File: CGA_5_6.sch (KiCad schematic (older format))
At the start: 34 parts, among them Q1 2N3904, U13 74LS08, U14 74S32, U15 74LS00, U20 74LS04, U21 74LS174, U24 74LS244, U41 74LS08, U42 74LS86, U43 74S74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

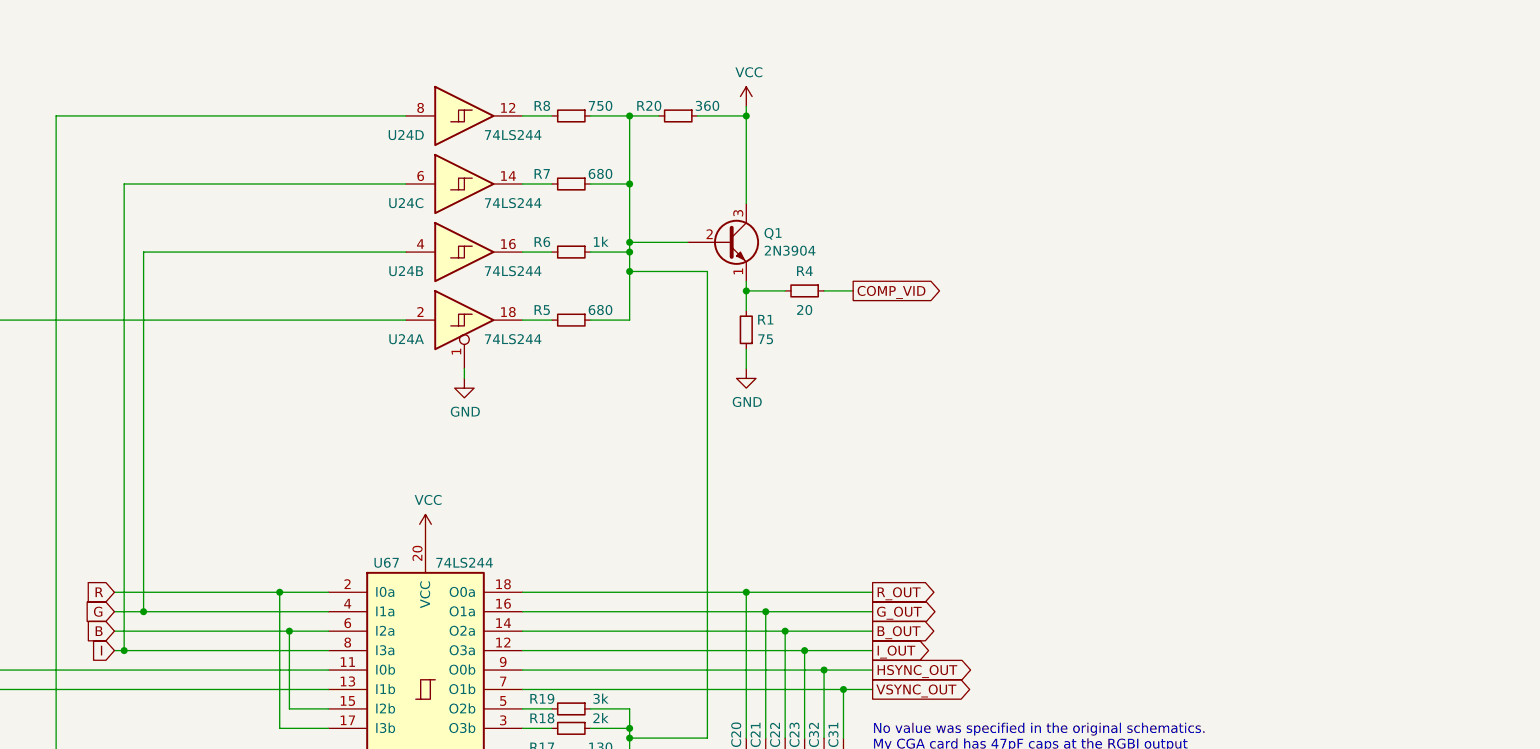
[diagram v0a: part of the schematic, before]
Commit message: Begin working on rev 0.2, for an easier "old" composite out mod
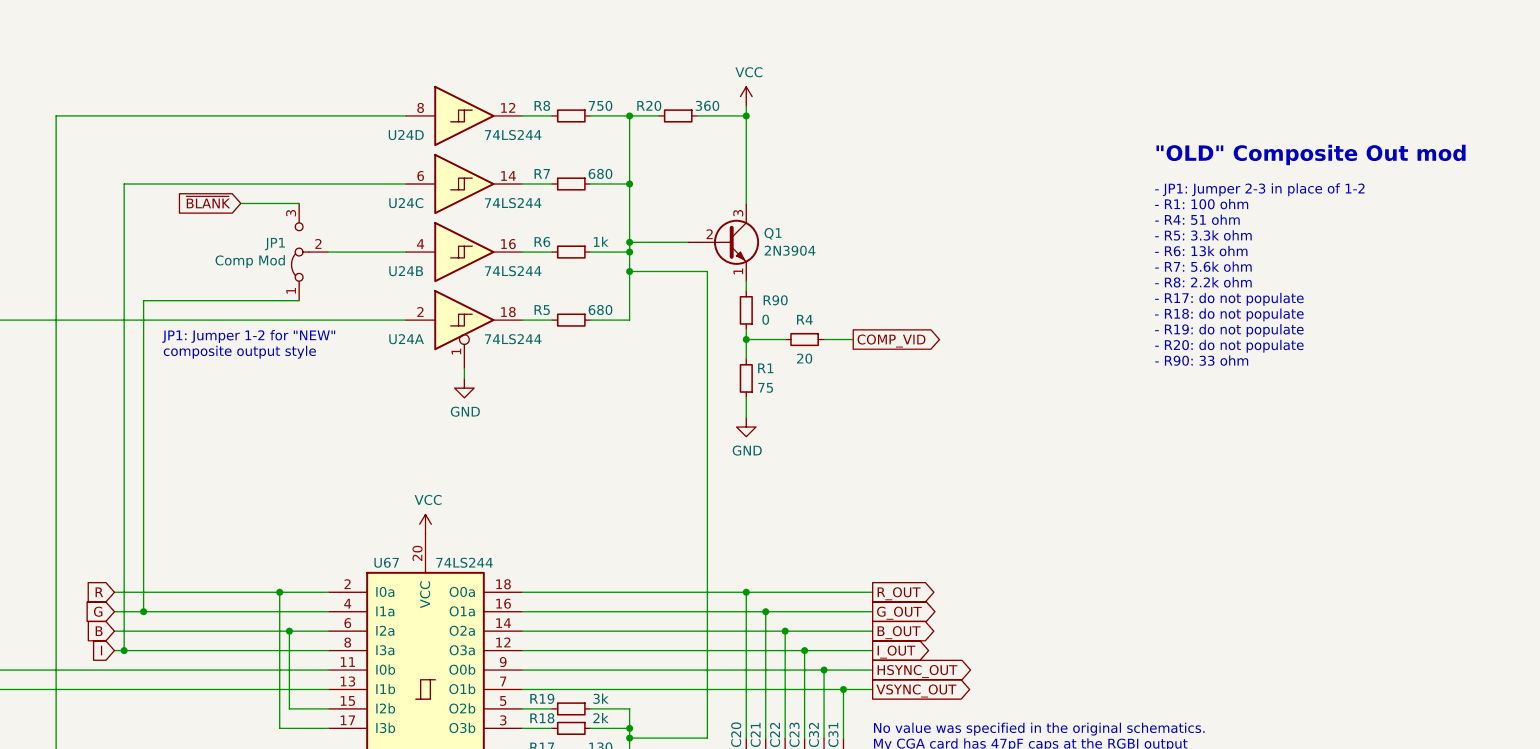
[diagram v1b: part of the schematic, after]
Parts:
- added JP1: Comp Mod, Jumper:SolderJumper-3_P1.3mm_Open_RoundedPad1.0x1.5mm_NumberLabels, symbol Jumper:Jumper_3_Bridged12
- added R90: 0, Resistor_THT:R_Axial_DIN0207_L6.3mm_D2.5mm_P10.16mm_Horizontal, symbol Device:R_Small
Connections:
- net G: now also JP1.1 (A); no longer U24.4
- net at R1.2, R4.2: now also R90.1; no longer Q1.1 (E)
- new net: JP1.2 (C), U24.4
- new net: Q1.1 (E), R90.2
- new net ~BLANK: JP1.3 (B)
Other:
- note added: ""OLD" Composite Out mod"
- note added: "- JP1: Jumper 2-3 in place of 1-2\n- R1: 100 ohm\n- R4: 51 ohm\n- R5: 3.3k ohm\n- R6: 13k ohm\n- R7: 5.6k ohm\n- R8: 2.2k ohm\n- R17: do not populate\n- R18: do not populate\n- R19: do not populate\n- R20: do not populate\n- R90: 33 ohm"
- note added: "JP1: Jumper 1-2 for "NEW"\ncomposite output style"
- moved on the sheet: R1, R4
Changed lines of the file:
@@
 Title ""
 Date ""
-Rev ""
+Rev "0.2"
 Comp ""
 Comment1 ""
@@
 Wire Wire Line
 	10600 5500 10900 5500
-$Comp
-L Device:R_Small R?
-U 1 1 6419FB7A
-P 11200 5950
-AR Path="/60463C10/6419FB7A" Ref="R?"  Part="1"
-AR Path="/60463CF3/6419FB7A" Ref="R1"  Part="1"
-F 0 "R1" H 11100 5900 50  0000 C CNN
-F 1 "75" H 11100 6000 50  0000 C CNN
-F 2 "Resistor_THT:R_Axial_DIN0207_L6.3mm_D2.5mm_P10.16mm_Horizontal" H 11200 5950 50  0001 C CNN
-F 3 "~" H 11200 5950 50  0001 C CNN
-	1    11200 5950
-	-1   0    0    1
-$EndComp
-Wire Wire Line
-	11200 5700 11200 5750
-$Comp
-L power:GND #PWR0198
-U 1 1 641B0622
-P 11200 6150
-F 0 "#PWR0198" H 11200 5900 50  0001 C CNN
-F 1 "GND" H 11205 5977 50  0000 C CNN
-F 2 "" H 11200 6150 50  0001 C CNN
-F 3 "" H 11200 6150 50  0001 C CNN
-	1    11200 6150
-	1    0    0    -1
-$EndComp
-Wire Wire Line
-	11200 6050 11200 6150
-$Comp
-L Device:R_Small R?
-U 1 1 641B7D8A
-P 11500 5750
-AR Path="/60463C10/641B7D8A" Ref="R?"  Part="1"
-AR Path="/60463CF3/641B7D8A" Ref="R4"  Part="1"
-F 0 "R4" V 11400 5750 50  0000 C CNN
-F 1 "20" V 11600 5750 50  0000 C CNN
-F 2 "Resistor_THT:R_Axial_DIN0207_L6.3mm_D2.5mm_P10.16mm_Horizontal" H 11500 5750 50  0001 C CNN
-F 3 "~" H 11500 5750 50  0001 C CNN
-	1    11500 5750
-	0    1    1    0
-$EndComp
-Wire Wire Line
-	11400 5750 11200 5750
-Connection ~ 11200 5750
-Wire Wire Line
-	11200 5750 11200 5850
-Text GLabel 11750 5750 2    50   Output ~ 0
-COMP_VID
-Wire Wire Line
-	11600 5750 11750 5750
+Wire Wire Line
+	11200 5950 11200 6000
+Wire Wire Line
+	11400 6000 11200 6000
 $Comp
 L 74xx:74LS125 U?
@@
 	8000 7600 9050 7600
 Wire Wire Line
-	8100 7400 8100 5550
-Wire Wire Line
-	8100 5550 9450 5550
+	8100 7400 8100 5800
 Connection ~ 8100 7400
 Wire Wire Line
@@
 	0    1    1    0
 $EndComp
+$Comp
+L Jumper:Jumper_3_Bridged12 JP1
+U 1 1 60CD53CC
+P 8900 5550
+F 0 "JP1" V 8946 5617 50  0000 L CNN
+F 1 "Comp Mod" V 8855 5617 50  0000 L CNN
+F 2 "Jumper:SolderJumper-3_P1.3mm_Open_RoundedPad1.0x1.5mm_NumberLabels" H 8900 5550 50  0001 C CNN
+F 3 "~" H 8900 5550 50  0001 C CNN
+	1    8900 5550
+	0    -1   -1   0
+$EndComp
+Wire Wire Line
+	9050 5550 9450 5550
+Wire Wire Line
+	8900 5800 8100 5800
+Text GLabel 8600 5300 0    50   Input ~ 0
+~BLANK
+Wire Wire Line
+	8900 5300 8600 5300
+Wire Wire Line
+	11600 6000 11750 6000
+Text GLabel 11750 6000 2    50   Output ~ 0
+COMP_VID
+$Comp
+L Device:R_Small R?
+U 1 1 641B7D8A
+P 11500 6000
+AR Path="/60463C10/641B7D8A" Ref="R?"  Part="1"
+AR Path="/60463CF3/641B7D8A" Ref="R4"  Part="1"
+F 0 "R4" V 11400 6000 50  0000 C CNN
+F 1 "20" V 11600 6000 50  0000 C CNN
+F 2 "Resistor_THT:R_Axial_DIN0207_L6.3mm_D2.5mm_P10.16mm_Horizontal" H 11500 6000 50  0001 C CNN
+F 3 "~" H 11500 6000 50  0001 C CNN
+	1    11500 6000
+	0    1    1    0
+$EndComp
+Connection ~ 11200 6000
+Wire Wire Line
+	11200 6000 11200 6100
+Wire Wire Line
+	11200 6300 11200 6400
+$Comp
+L power:GND #PWR0198
+U 1 1 641B0622
+P 11200 6400
+F 0 "#PWR0198" H 11200 6150 50  0001 C CNN
+F 1 "GND" H 11205 6227 50  0000 C CNN
+F 2 "" H 11200 6400 50  0001 C CNN
+F 3 "" H 11200 6400 50  0001 C CNN
+	1    11200 6400
+	1    0    0    -1
+$EndComp
+$Comp
+L Device:R_Small R?
+U 1 1 6419FB7A
+P 11200 6200
+AR Path="/60463C10/6419FB7A" Ref="R?"  Part="1"
+AR Path="/60463CF3/6419FB7A" Ref="R1"  Part="1"
+F 0 "R1" H 11100 6150 50  0000 C CNN
+F 1 "75" H 11100 6250 50  0000 C CNN
+F 2 "Resistor_THT:R_Axial_DIN0207_L6.3mm_D2.5mm_P10.16mm_Horizontal" H 11200 6200 50  0001 C CNN
+F 3 "~" H 11200 6200 50  0001 C CNN
+	1    11200 6200
+	-1   0    0    1
+$EndComp
+$Comp
+L Device:R_Small R?
+U 1 1 60E2BE95
+P 11200 5850
+AR Path="/60463C10/60E2BE95" Ref="R?"  Part="1"
+AR Path="/60463CF3/60E2BE95" Ref="R90"  Part="1"
+F 0 "R90" H 11050 5800 50  0000 C CNN
+F 1 "0" H 11100 5900 50  0000 C CNN
+F 2 "Resistor_THT:R_Axial_DIN0207_L6.3mm_D2.5mm_P10.16mm_Horizontal" H 11200 5850 50  0001 C CNN
+F 3 "~" H 11200 5850 50  0001 C CNN
+	1    11200 5850
+	-1   0    0    1
+$EndComp
+Wire Wire Line
+	11200 5750 11200 5700
+Text Notes 13300 5100 0    79   ~ 16
+"OLD" Composite Out mod
+Text Notes 13300 6150 0    50   ~ 0
+- JP1: Jumper 2-3 in place of 1-2\n- R1: 100 ohm\n- R4: 51 ohm\n- R5: 3.3k ohm\n- R6: 13k ohm\n- R7: 5.6k ohm\n- R8: 2.2k ohm\n- R17: do not populate\n- R18: do not populate\n- R19: do not populate\n- R20: do not populate\n- R90: 33 ohm
+Text Notes 8200 6100 0    50   ~ 0
+JP1: Jumper 1-2 for "NEW"\ncomposite output style
 $EndSCHEMATC
